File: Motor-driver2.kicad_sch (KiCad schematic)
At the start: 49 parts, among them J12 PINHD_1x4_Male, J15 PINHD_1x4_Male, U4 DRV8825PWP, U5 DRV8825PWP

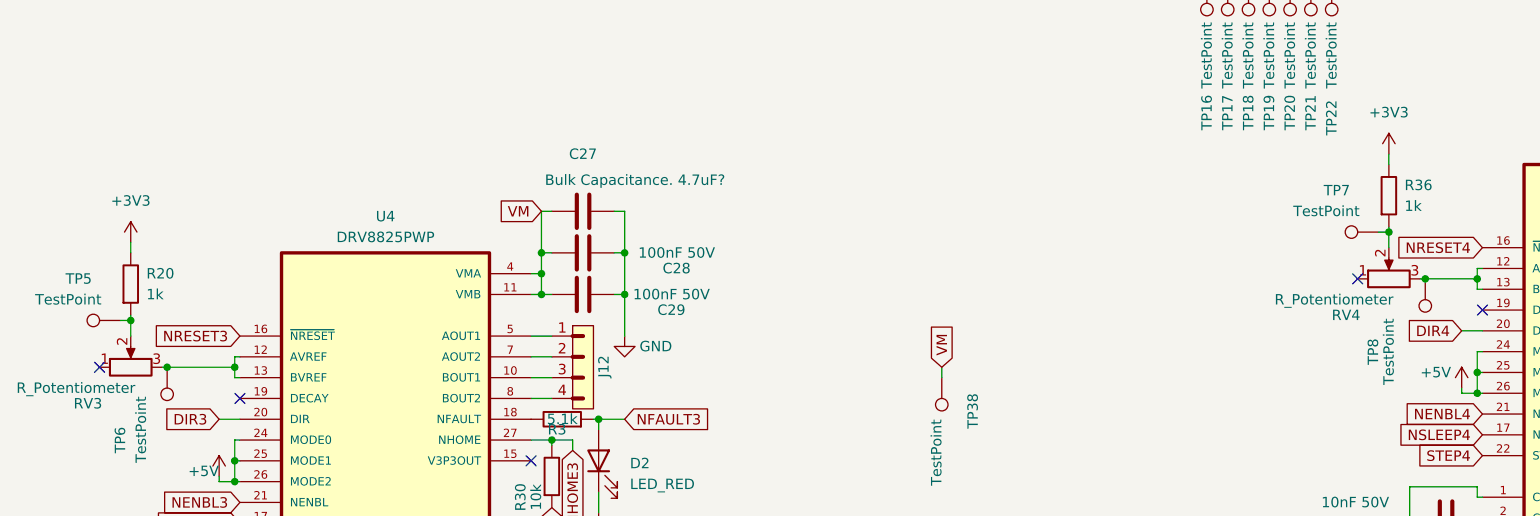
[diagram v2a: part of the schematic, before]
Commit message: deleted unnecessary testpoints
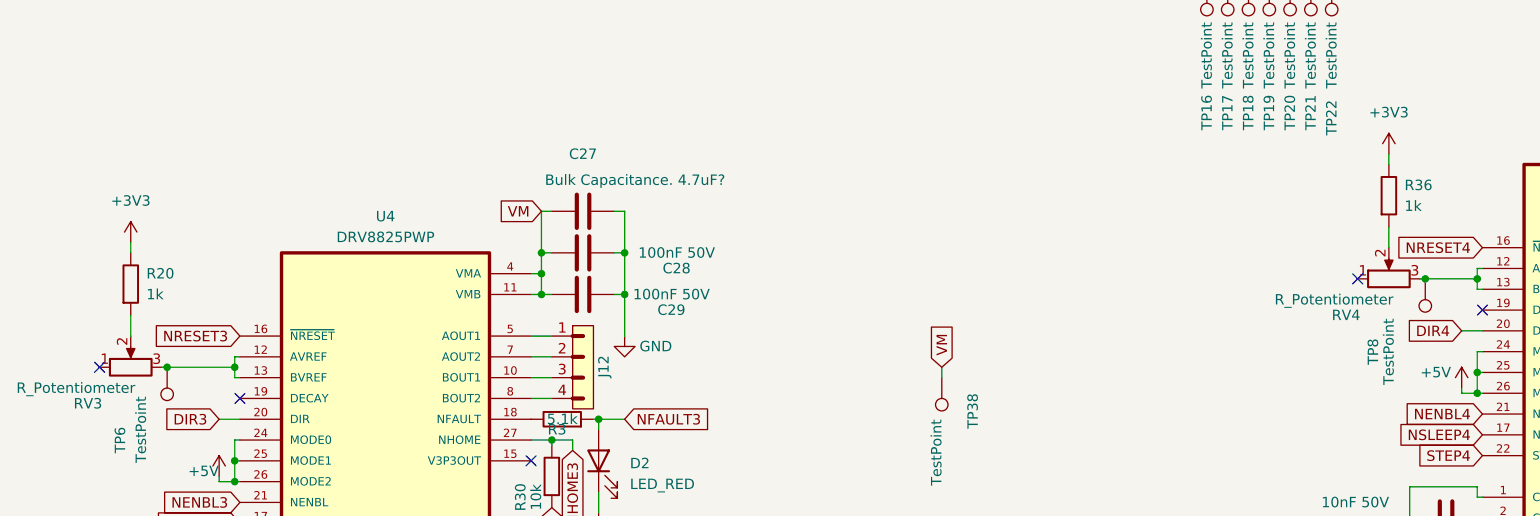
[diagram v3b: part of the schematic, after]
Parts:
- removed TP5, TP7: TestPoint, TestPoint:TestPoint_Pad_D2.5mm, symbol Connector:TestPoint
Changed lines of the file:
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@@
 (kicad_sch (version 20230121) (generator eeschema)
   (paper "A4")
-  (junction (at 192.405 85.725) (diameter 0) (color 0 0 0 0)
-  )
   (junction (at 90.17 111.125) (diameter 0) (color 0 0 0 0)
   )
@@
   )
   (junction (at 43.18 102.235) (diameter 0) (color 0 0 0 0)
-  )
-  (junction (at 38.735 96.52) (diameter 0) (color 0 0 0 0)
   )
   (junction (at 199.39 147.955) (diameter 0) (color 0 0 0 0)
@@
     (stroke (width 0) (type default))
   )
-  (wire (pts (xy 192.405 85.09) (xy 192.405 85.725))
-    (stroke (width 0) (type default))
-  )
   (wire (pts (xy 199.39 147.955) (xy 203.835 147.955))
     (stroke (width 0) (type default))
@@
     (stroke (width 0) (type default))
   )
-  (wire (pts (xy 191.135 85.725) (xy 192.405 85.725))
-    (stroke (width 0) (type default))
-  )
   (wire (pts (xy 51.435 113.665) (xy 52.07 113.665))
     (stroke (width 0) (type default))
@@
     (stroke (width 0) (type default))
   )
-  (wire (pts (xy 38.735 96.52) (xy 38.735 98.425))
+  (wire (pts (xy 38.735 95.885) (xy 38.735 98.425))
     (stroke (width 0) (type default))
   )
@@
     (stroke (width 0) (type default))
   )
-  (wire (pts (xy 192.405 85.725) (xy 192.405 87.63))
+  (wire (pts (xy 192.405 85.09) (xy 192.405 87.63))
     (stroke (width 0) (type default))
   )
@@
     (stroke (width 0) (type default))
   )
-  (wire (pts (xy 38.735 95.885) (xy 38.735 96.52))
-    (stroke (width 0) (type default))
-  )
   (wire (pts (xy 203.2 102.87) (xy 203.2 105.41))
     (stroke (width 0) (type default))
@@
   )
   (wire (pts (xy 180.975 26.67) (xy 182.88 26.67))
-    (stroke (width 0) (type default))
-  )
-  (wire (pts (xy 37.465 96.52) (xy 38.735 96.52))
     (stroke (width 0) (type default))
   )
@@
     )
   )
-  (symbol (lib_id "Connector:TestPoint") (at 191.135 85.725 90) (unit 1)
-    (in_bom yes) (on_board yes) (dnp no)
-    (property "Reference" "TP7" (at 186.055 80.645 90)
-      (effects (font (size 1.27 1.27)))
-    )
-    (property "Value" "TestPoint" (at 184.785 83.185 90)
-      (effects (font (size 1.27 1.27)))
-    )
-    (property "Footprint" "TestPoint:TestPoint_Pad_D2.5mm" (at 191.135 80.645 0)
-      (effects (font (size 1.27 1.27)) hide)
-    )
-    (property "Datasheet" "~" (at 191.135 80.645 0)
-      (effects (font (size 1.27 1.27)) hide)
-    )
-    (pin "1")
-    (instances
-      (project "Doodle Drive"
-        (path "/3ec634aa-8c09-482d-9325-2288a4dbd68b/4a4951fa-be57-4d48-97a5-6be750b353b5"
-          (reference "TP7") (unit 1)
-        )
-      )
-    )
-  )
   (symbol (lib_id "Connector:TestPoint") (at 43.18 102.235 180) (unit 1)
     (in_bom yes) (on_board yes) (dnp no)
@@
         )
       )
-    )
-  )
-  (symbol (lib_id "Connector:TestPoint") (at 37.465 96.52 90) (unit 1)
-    (in_bom yes) (on_board yes) (dnp no)
-    (property "Reference" "TP5" (at 32.385 91.44 90)
-      (effects (font (size 1.27 1.27)))
-    )
-    (property "Value" "TestPoint" (at 31.115 93.98 90)
-      (effects (font (size 1.27 1.27)))
-    )
-    (property "Footprint" "TestPoint:TestPoint_Pad_D2.5mm" (at 37.465 91.44 0)
-      (effects (font (size 1.27 1.27)) hide)
-    )
-    (property "Datasheet" "~" (at 37.465 91.44 0)
-      (effects (font (size 1.27 1.27)) hide)
-    )
-    (pin "1")
-    (instances
-      (project "Doodle Drive"
-        (path "/3ec634aa-8c09-482d-9325-2288a4dbd68b/4a4951fa-be57-4d48-97a5-6be750b353b5"
-          (reference "TP5") (unit 1)
-        )
-      )

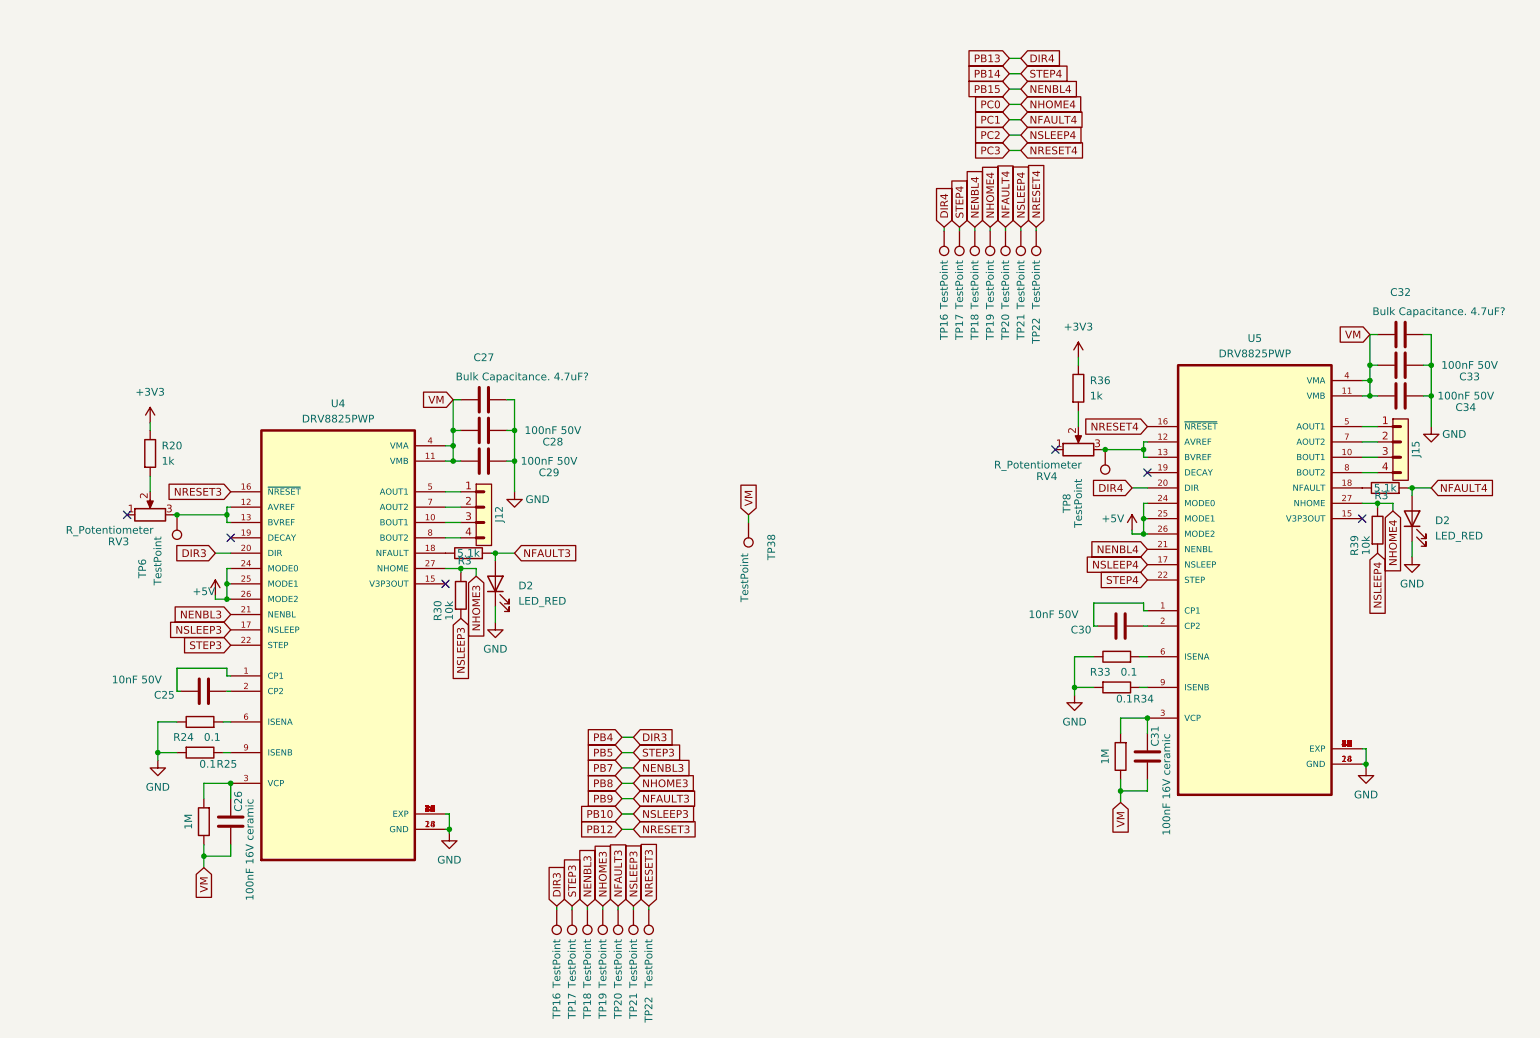
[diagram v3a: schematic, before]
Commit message: fixed voltage dividers, roughly arrangenged components on pcb, set up 3V3 and GND area
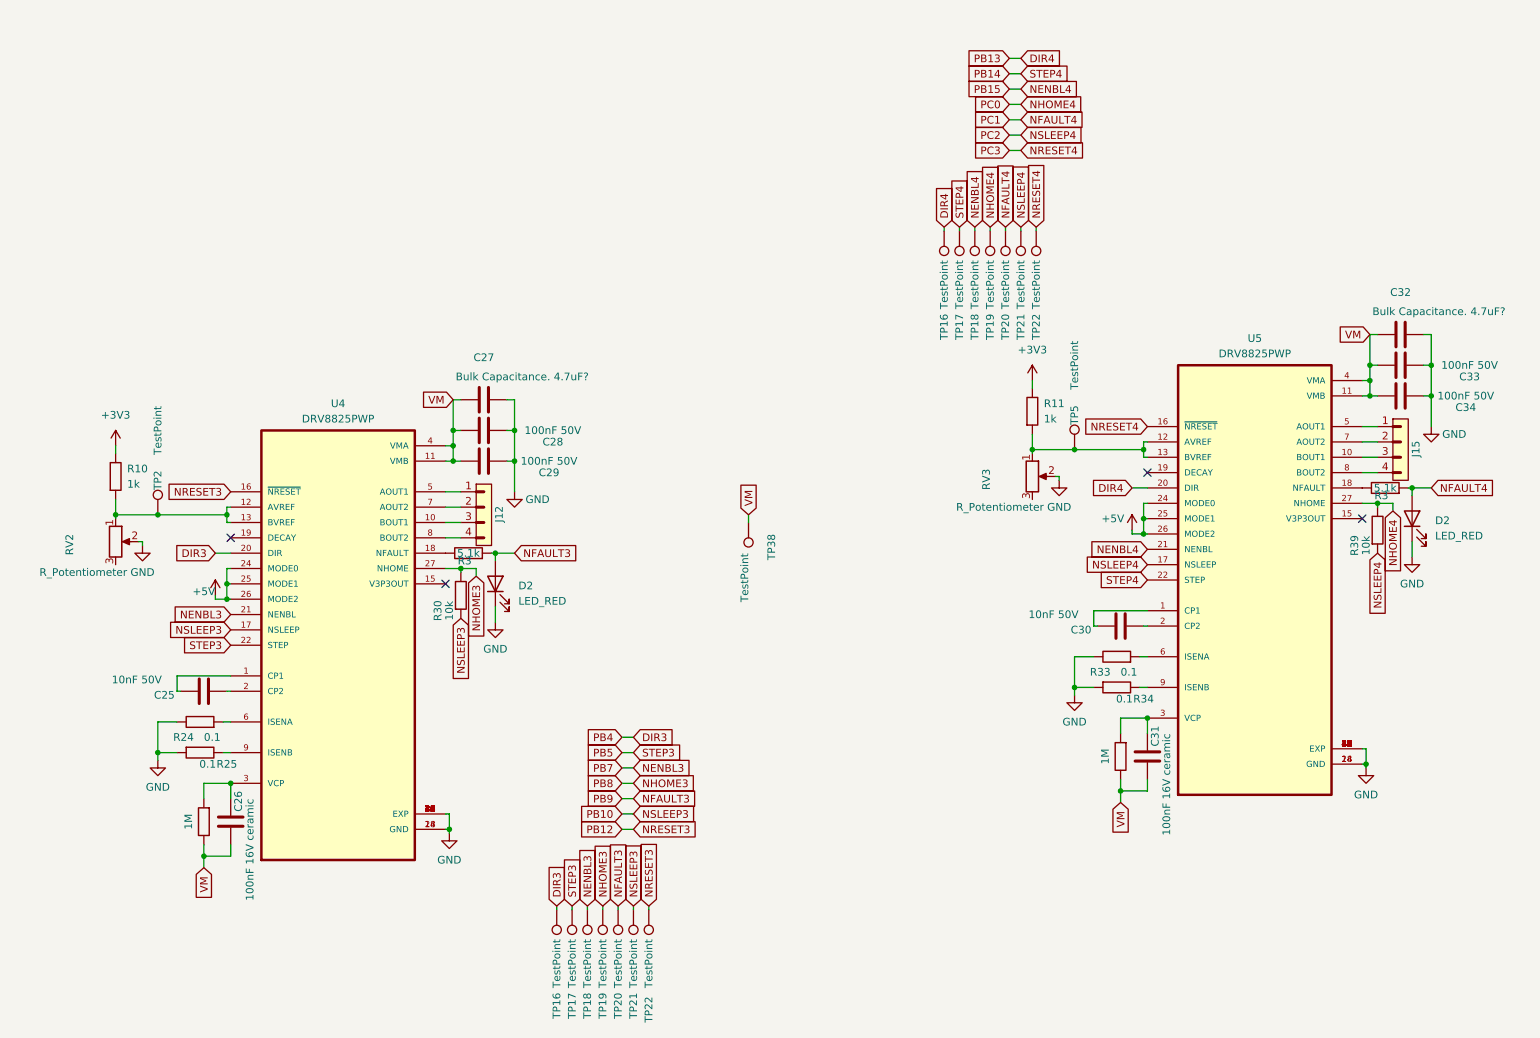
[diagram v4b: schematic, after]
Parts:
- removed R20, R36: 1k, Resistor_SMD:R_0805_2012Metric, symbol PCM_SL_Devices:Resistor
- removed RV4: R_Potentiometer, Potentiometer_THT:Potentiometer_ACP_CA6-H2,5_Horizontal, symbol Device:R_Potentiometer
- removed TP6, TP8: TestPoint, TestPoint:TestPoint_Pad_D2.5mm, symbol Connector:TestPoint
- added R10, R11: 1k, Resistor_SMD:R_0805_2012Metric, symbol PCM_SL_Devices:Resistor
- added RV2: R_Potentiometer, Potentiometer_THT:Potentiometer_ACP_CA6-H2,5_Horizontal, symbol Device:R_Potentiometer
- added TP2, TP5: TestPoint, TestPoint:TestPoint_Pad_D2.5mm, symbol Connector:TestPoint
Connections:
- net +3V3: now also R10.2, R11.2
- net GND: now also RV3.2, RV2.2
- net at U4.12 (AVREF), U4.13 (BVREF): now also R10.1, RV2.1, TP2.1; no longer RV3.3
- net at U5.12 (AVREF), U5.13 (BVREF): now also RV3.1, R11.1, TP5.1
- no-connect marks 6 -> 4
